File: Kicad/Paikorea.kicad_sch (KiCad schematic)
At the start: 49 parts, among them J1 AudioJack3, J2 TPS43-201A-S, J4 AudioJack3, K10 PG1316S, K11 PG1316S, K12 PG1316S, K13 PG1316S, K14 PG1316S, K15 PG1316S, K16 PG1316S, K17 PG1316S, K18 PG1316S, K19 PG1316S, K20 PG1316S, K21 PG1316S, K22 PG1316S, K4 PG1316S, K5 PG1316S, K6 PG1316S, K7 PG1316S, K8 PG1316S, K9 PG1316S, U1 RP2040-Zero, U2 RP2040-Zero

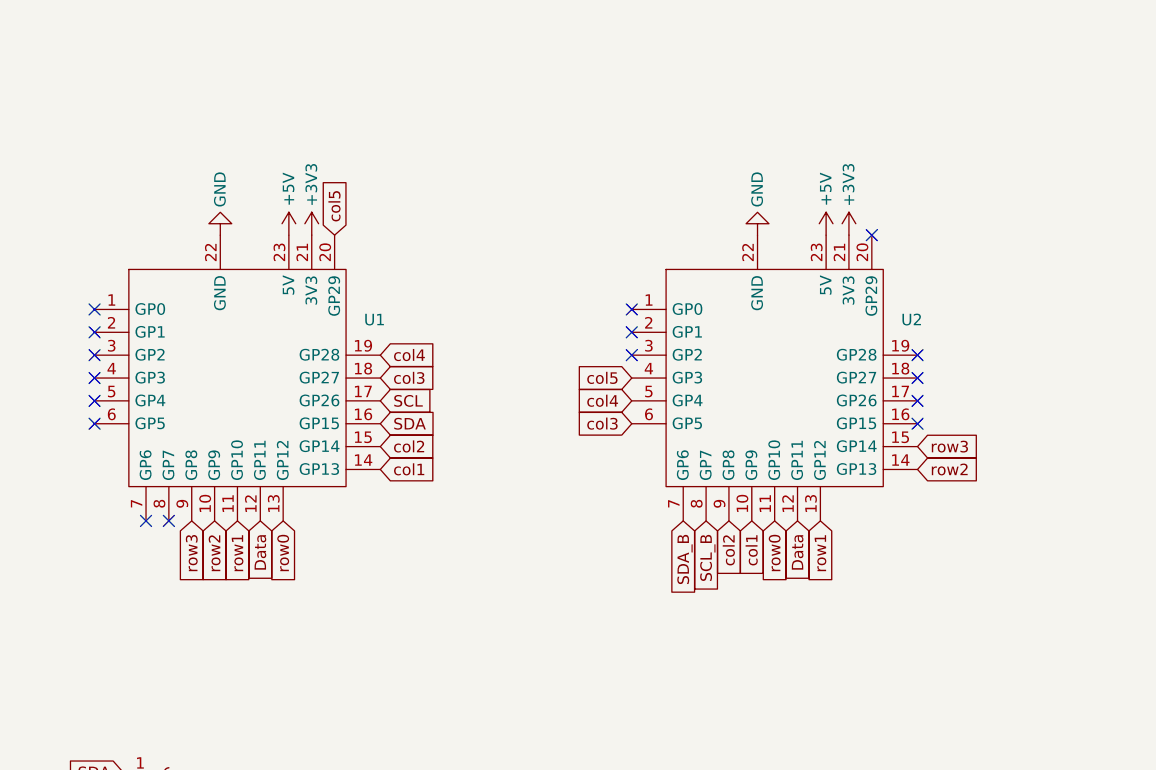
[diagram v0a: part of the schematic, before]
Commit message: RP2040-Zero: use footprint/RP2040-Zero geometry, same GPIO numbers on front/back
- U1 (F) / U2 (B): new footprint Paikorea:RP2040-Zero_UpsideDown, derived from
  footprint/RP2040-Zero.kicad_mod (mirrored for upside-down mounting, holes removed -> SMD pads)
- Both modules now use the same GPIO numbers:
  GP0 col5, GP1 col4, GP2 col3, GP3 col2, GP4 col1, GP5 row0, GP6 row1, GP7 row2,
  GP8 SDA, GP9 SCL (I2C0), GP10 row3, GP11 Data
- Rerouted MCU area: left (F) fan-out crosses under the module and joins the right (B)
  fan-out through a via ladder; I2C/3V3/GND to J2, 5V/Data to TRRS
- Zone fills cleared (refill with B)

Co-Authored-By: Claude Opus 5.5 <noreply@anthropic.com>
Claude-Session: https://claude.ai/code/session_01CM6fo4n92yZJeCtkGbFXPU
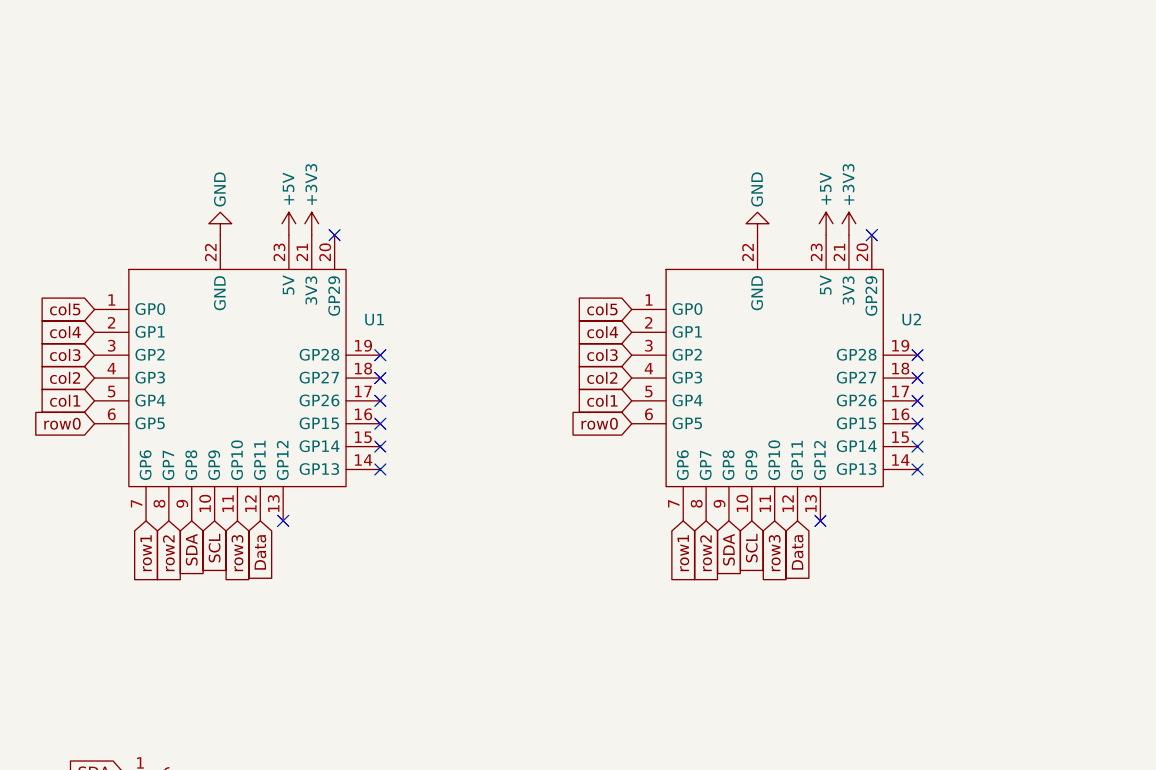
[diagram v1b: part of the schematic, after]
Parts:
- U1, U2: footprint Paikorea:RP2040_Zero_UpsideDown -> Paikorea:RP2040-Zero_UpsideDown
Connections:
- net SCL_B is gone; now on net row2: U2.8 (GP7)
- net SDA_B is gone; now on net row1: U2.7 (GP6)
- net SCL: now also U1.10 (GP9), U2.10 (GP9); no longer U1.17 (GP26)
- net SDA: now also U1.9 (GP8), U2.9 (GP8); no longer U1.16 (GP15)
- net col1: now also U1.5 (GP4), U2.5 (GP4); no longer U1.14 (GP13), U2.10 (GP9)
- net col2: now also U1.4 (GP3), U2.4 (GP3); no longer U1.15 (GP14), U2.9 (GP8)
- net col3: now also U1.3 (GP2), U2.3 (GP2); no longer U1.18 (GP27), U2.6 (GP5)
- net col4: now also U1.2 (GP1), U2.2 (GP1); no longer U1.19 (GP28), U2.5 (GP4)
- net col5: now also U1.1 (GP0), U2.1 (GP0); no longer U1.20 (GP29), U2.4 (GP3)
- net row0: now also U1.6 (GP5), U2.6 (GP5); no longer U1.13 (GP12), U2.11 (GP10)
- net row1: now also U1.7 (GP6); no longer U1.11 (GP10), U2.13 (GP12)
- net row2: now also U1.8 (GP7); no longer U1.10 (GP9), U2.14 (GP13)
- net row3: now also U1.11 (GP10), U2.11 (GP10); no longer U1.9 (GP8), U2.15 (GP14)
